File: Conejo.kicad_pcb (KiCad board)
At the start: 4 copper layers, 130.3 x 112.5 mm, 104 parts, among them J1 BATT, J2 HRO_TYPE-C-31-M-12, J3 JTAG_TC2030, J4 RGB, Q1 2N7002, Q2 2N7002, Q3 AO3407, SW1 POWER, SW10 MX Hotswap, SW11 MX Hotswap, SW12 MX Hotswap, SW13 MX Hotswap, SW14 MX Hotswap, SW15 MX Hotswap, SW16 MX Hotswap, SW17 MX Hotswap, SW18 MX Hotswap, SW19 MX Hotswap, SW2 MX Hotswap, SW20 MX Hotswap, SW21 MX Hotswap, SW22 MX Hotswap, SW23 MX Hotswap, SW24 MX Hotswap, SW25 MX Hotswap, SW26 MX Hotswap, SW27 MX Hotswap, SW28 MX Hotswap, SW29 RESET, SW3 MX Hotswap, SW4 MX Hotswap, SW5 MX Hotswap, SW6 MX Hotswap, SW7 MX Hotswap, SW8 MX Hotswap, SW9 MX Hotswap, U1 BQ24075RGT, U2 MAX17048, U3 SRV05-4, U4 MS88SF3

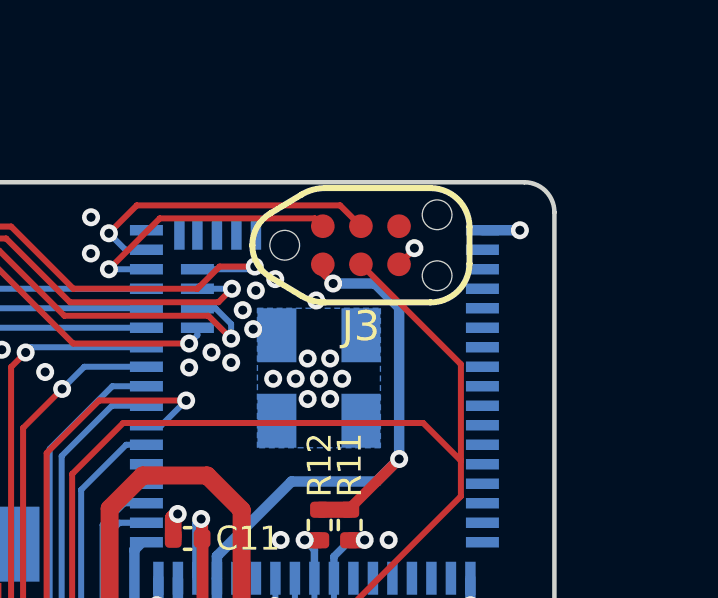
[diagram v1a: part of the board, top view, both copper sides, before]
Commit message: refactor(pcb): Update paths to 3D models, whole board .STEP
Delete EVQPU-LC-02K.STEP
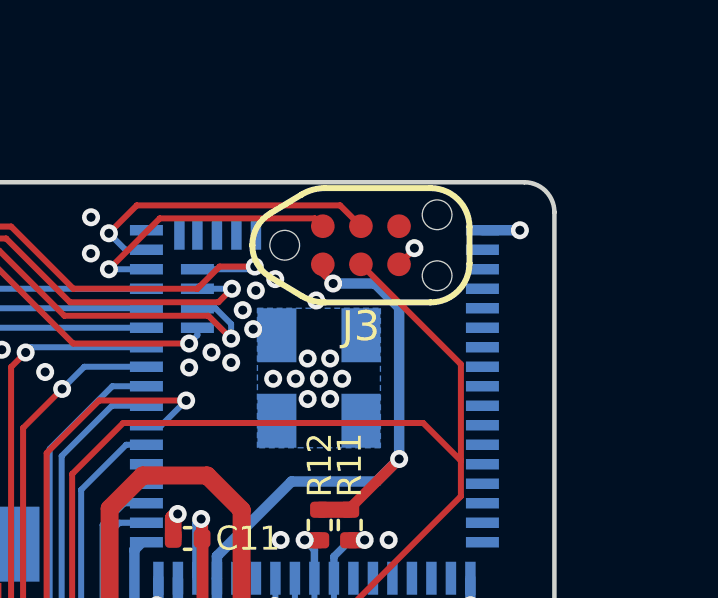
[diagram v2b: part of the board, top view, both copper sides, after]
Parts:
- U4: value MS88SF3 -> MS88SF3 nRF52840 Module
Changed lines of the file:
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@@
     (fp_arc (start 2.319501 -1.9055) (mid 3.23874 -1.524738) (end 3.6195 -0.605499) (layer "F.SilkS") (width 0.2))
     (fp_arc (start -3.6195 -0.008049) (mid -3.461104 -0.610529) (end -3.026877 -1.057203) (layer "F.SilkS") (width 0.2))
-    (fp_arc (start 3.6195 0.605498) (mid 3.23874 1.524738) (end 2.3195 1.9055) (layer "F.SilkS") (width 0.2))
+    (fp_arc (start 3.6195 0.605498) (mid 3.238739 1.524738) (end 2.3195 1.9055) (layer "F.SilkS") (width 0.2))
     (fp_arc (start -1.976732 -1.690178) (mid -1.604252 -1.850667) (end -1.202392 -1.9055) (layer "F.SilkS") (width 0.2))
     (fp_arc (start -1.202392 1.9055) (mid -1.604252 1.850667) (end -1.976732 1.690178) (layer "F.SilkS") (width 0.2))
@@
       (effects (font (size 0.4 0.4) (thickness 0.06)) (justify mirror))
     )
+    (fp_line (start -2.1 0.95) (end -2.1 1.56) (layer "B.SilkS") (width 0.12))
     (fp_line (start -2.1 1.56) (end 0.8 1.56) (layer "B.SilkS") (width 0.12))
-    (fp_line (start -2.1 0.95) (end -2.1 1.56) (layer "B.SilkS") (width 0.12))
     (fp_line (start 0 -1.56) (end -0.8 -1.56) (layer "B.SilkS") (width 0.12))
     (fp_line (start 0 -1.56) (end 0.8 -1.56) (layer "B.SilkS") (width 0.12))
+    (fp_line (start -2.05 1.7) (end -2.05 -1.7) (layer "B.CrtYd") (width 0.05))
     (fp_line (start 2.05 1.7) (end -2.05 1.7) (layer "B.CrtYd") (width 0.05))
     (fp_line (start -2.05 -1.7) (end 2.05 -1.7) (layer "B.CrtYd") (width 0.05))
     (fp_line (start 2.05 -1.7) (end 2.05 1.7) (layer "B.CrtYd") (width 0.05))
-    (fp_line (start -2.05 1.7) (end -2.05 -1.7) (layer "B.CrtYd") (width 0.05))
+    (fp_line (start -0.4 1.45) (end 0.8 1.45) (layer "B.Fab") (width 0.1))
+    (fp_line (start -0.8 -1.45) (end -0.8 1.05) (layer "B.Fab") (width 0.1))
+    (fp_line (start 0.8 -1.45) (end -0.8 -1.45) (layer "B.Fab") (width 0.1))
     (fp_line (start -0.8 1.05) (end -0.4 1.45) (layer "B.Fab") (width 0.1))
     (fp_line (start 0.8 1.45) (end 0.8 -1.45) (layer "B.Fab") (width 0.1))
-    (fp_line (start 0.8 -1.45) (end -0.8 -1.45) (layer "B.Fab") (width 0.1))
-    (fp_line (start -0.8 -1.45) (end -0.8 1.05) (layer "B.Fab") (width 0.1))
-    (fp_line (start -0.4 1.45) (end 0.8 1.45) (layer "B.Fab") (width 0.1))
     (pad "1" smd roundrect (at -1.175 0.95 270) (size 1.25 0.6) (layers "B.Cu" "B.Paste" "B.Mask") (roundrect_rratio 0.25)
       (net 103 "unconnected-(U3-Pad1)") (pinfunction "IO1") (pintype "passive"))
@@
       (effects (font (size 1 1) (thickness 0.15)) (justify mirror))
     )
-    (fp_text value "MS88SF3" (at 2.14 -12.385) (layer "B.Fab")
+    (fp_text value "MS88SF3 nRF52840 Module" (at 2.14 -12.385) (layer "B.Fab")
       (effects (font (size 1 1) (thickness 0.15)) (justify mirror))
     )
@@
     (fp_line (start 5 7) (end 7 7) (layer "Dwgs.User") (width 0.15))
     (fp_line (start 7 -7) (end 7 -5) (layer "Dwgs.User") (width 0.15))
+    (fp_line (start -5 7) (end -7 7) (layer "Dwgs.User") (width 0.15))
     (fp_line (start -7 7) (end -7 5) (layer "Dwgs.User") (width 0.15))
     (fp_line (start -5 7) (end -7 7) (layer "Dwgs.User") (width 0.15))
     (fp_line (start 5 -7) (end 7 -7) (layer "Dwgs.User") (width 0.15))
     (fp_line (start 7 5) (end 7 7) (layer "Dwgs.User") (width 0.15))
-    (fp_line (start -5 7) (end -7 7) (layer "Dwgs.User") (width 0.15))
     (fp_line (start -7 7) (end -7 5) (layer "Dwgs.User") (width 0.15))
     (fp_rect (start -14.2875 9.525) (end 14.2875 -9.525) (layer "Dwgs.User") (width 0.12) (fill none))
@@
     (fp_arc (start 6.5 4.5) (mid 5.767767 6.267767) (end 4 7) (layer "B.CrtYd") (width 0.127))
     (fp_line (start 5.3 7) (end 5.3 2.6) (layer "F.CrtYd") (width 0.127))
+    (fp_line (start -6.5 0.6) (end -2.4 0.6) (layer "F.CrtYd") (width 0.127))
     (fp_line (start -0.4 2.6) (end 5.3 2.6) (layer "F.CrtYd") (width 0.127))
-    (fp_line (start -6.5 0.6) (end -2.4 0.6) (layer "F.CrtYd") (width 0.127))
     (fp_line (start -6.5 4.5) (end -6.5 0.6) (layer "F.CrtYd") (width 0.127))
     (fp_line (start 5.3 7) (end -4 7) (layer "F.CrtYd") (width 0.127))
@@
     (pad "" smd rect (at 5.815 5.08 255) (size 2.55 2.5) (layers "F.Paste" "F.Mask"))
     (pad "" np_thru_hole circle (at 0 0 255) (size 3.9878 3.9878) (drill 3.9878) (layers *.Cu *.Mask))
-    (pad "" smd rect (at -7.085 2.54 75) (size 2.55 2.5) (layers "F.Paste" "F.Mask"))
     (pad "" smd rect (at -5.815 5.08 255) (size 2.55 2.5) (layers "B.Paste" "B.Mask"))
     (pad "" smd rect (at 7.085 2.54 255) (size 2.55 2.5) (layers "B.Paste" "B.Mask"))
     (pad "" smd rect (at 5.815 5.08 255) (size 2.55 2.5) (layers "F.Paste" "F.Mask"))
+    (pad "" smd rect (at -7.085 2.54 75) (size 2.55 2.5) (layers "F.Paste" "F.Mask"))
     (pad "1" smd rect (at -5.341 5.08 255) (size 3.498 2.5) (layers "B.Cu")
       (net 40 "COL6") (pinfunction "1") (pintype "passive"))

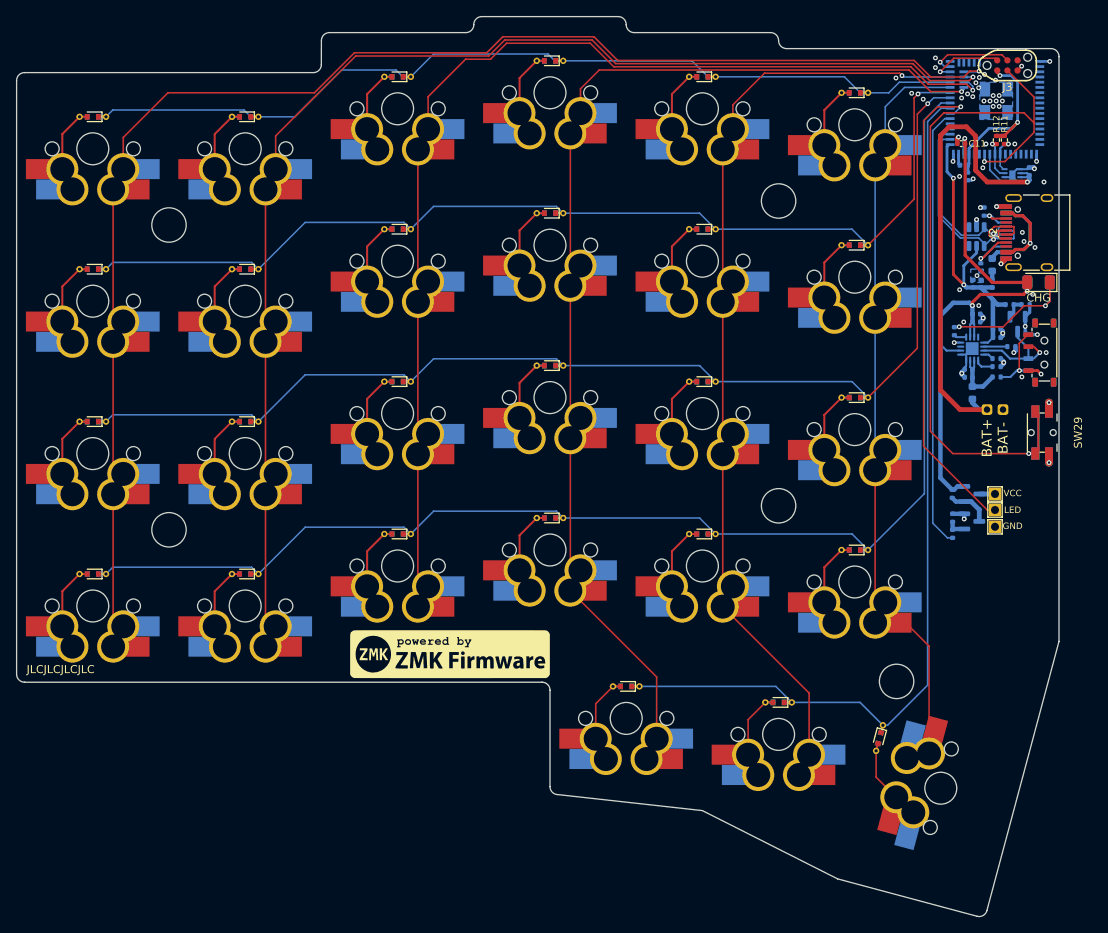
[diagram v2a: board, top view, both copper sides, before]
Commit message: feat(pcb): Version 0.2.2
- Update MS88SF3 footprint
- Create thumb cluster silksscreen
- Separate NTPH and PTH drill files
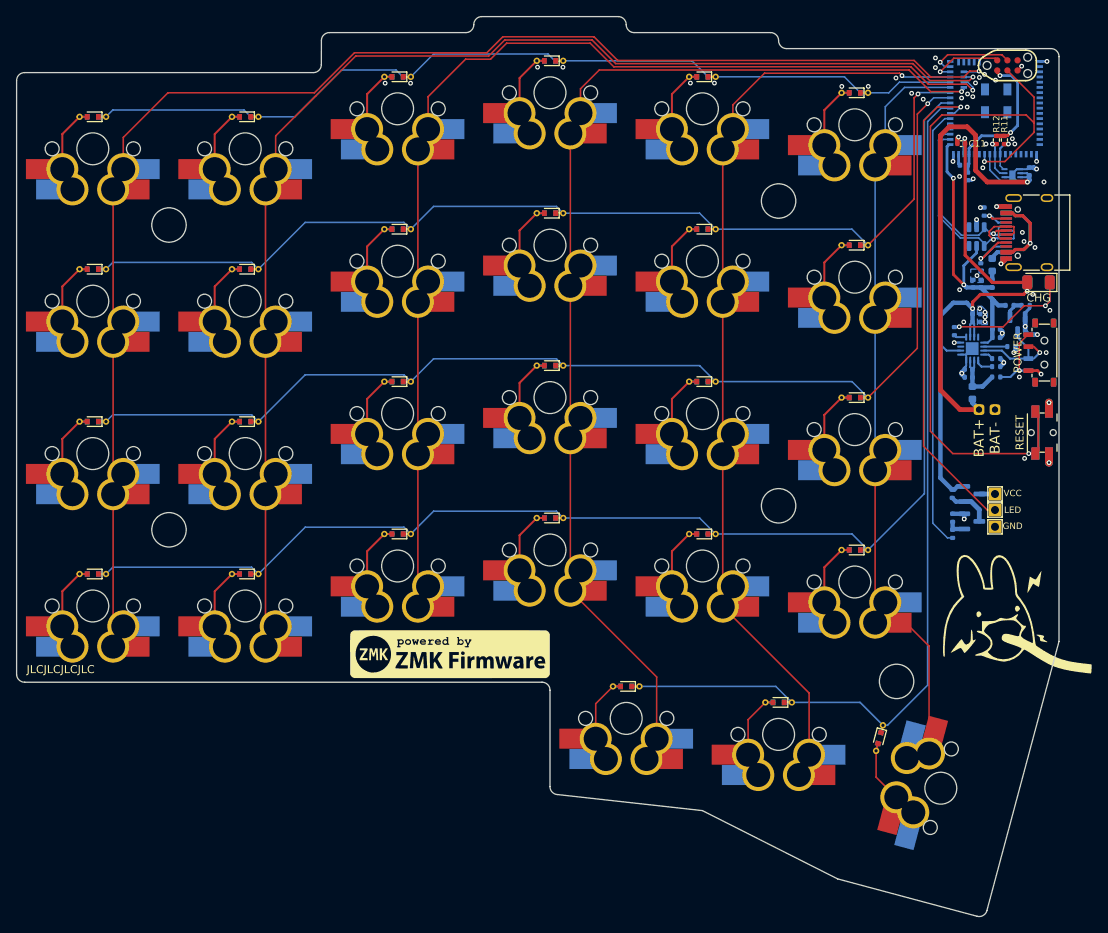
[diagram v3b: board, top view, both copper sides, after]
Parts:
- added G***: LOGO, Conejo:ConejoSilk, F.Cu at (114.8, 61.8)
- U4: value MS88SF3 nRF52840 Module -> MS88SF3; footprint Conejo:MS88SF3 -> Conejo:MS88SF3_PeteJohanson
- moved J1 1.00 mm to (111.8, 34.6)
- moved R2 0.10 mm to (116.6, 21.6)
- moved R1 0.10 mm to (114.6, 21.6)
- moved C1 0.08 mm to (112.9, 24.6)
- moved C2 0.08 mm to (112.9, 25.6)
- moved Q1 0.05 mm to (115.6, 24.0)
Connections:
- net SWDCLK renamed SWCLK
- U4 pad 61: GND -> (no net)
- U4 pad 62: GND -> (no net)
- U4 pad 63: GND -> (no net)
- U4 pad 64: GND -> (no net)
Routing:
- net +BATT: track 61.4 -> 59.4 mm
- net VDD: track 22.3 -> 21.2 mm
- net GND: track 39.8 -> 38.7 mm, vias 59 -> 64
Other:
- rule pad_to_mask_clearance: 0.05 -> 0
- board text added: "RESET"

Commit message: fix(pcb): Finalize part selection
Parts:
- L1: footprint Inductor_SMD:L_0402_1005Metric -> Inductor_SMD:L_0603_1608Metric
- moved C11 1.17 mm to (108.5, 2.52)
- moved C10 0.60 mm to (109.7, 5.97)
- moved L1 0.28 mm to (108.9, 4.33)
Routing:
- net VDDH: track 73.8 -> 72.1 mm
- net +BATT: track 59.4 -> 57.8 mm

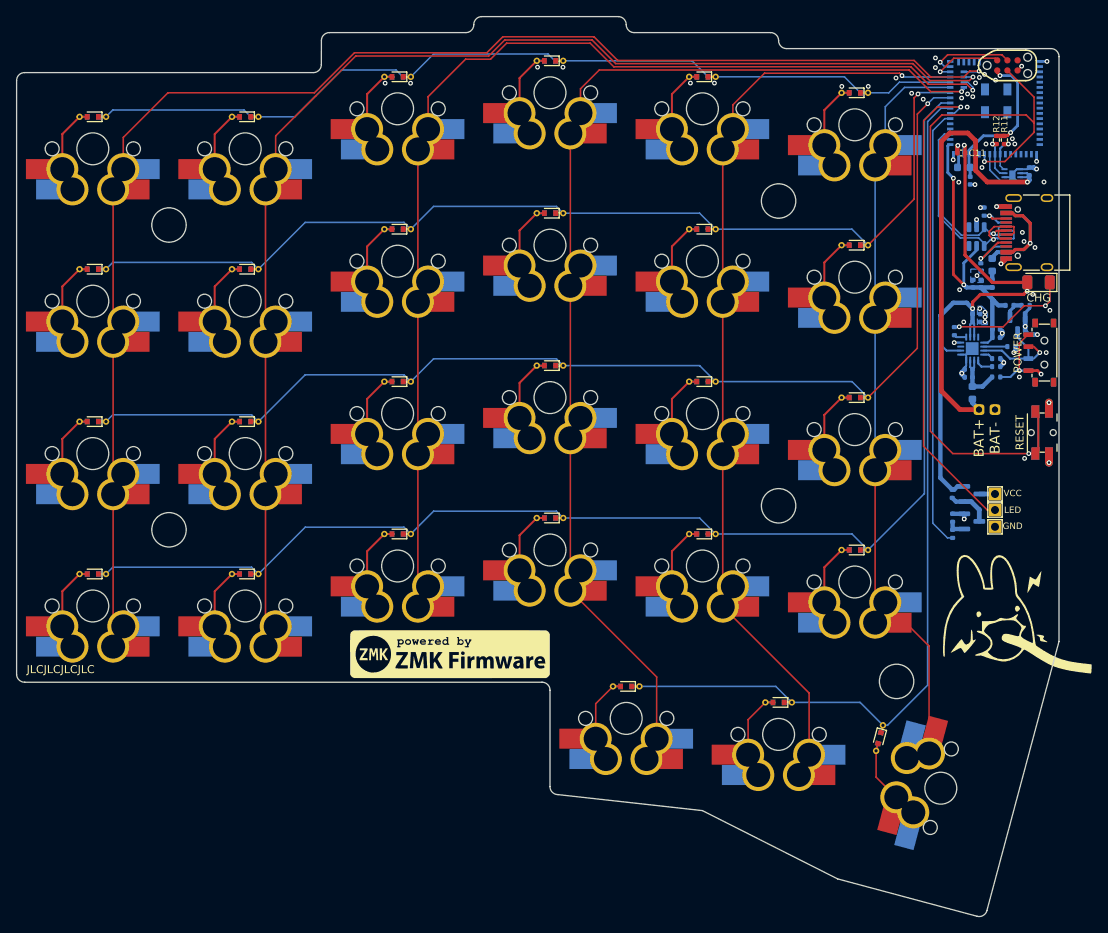
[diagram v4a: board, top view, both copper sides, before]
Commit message: feat(pcb): Version 0.2.3
- Switched vertical traces on matrix to back copper
- Added GND vias for all diodes
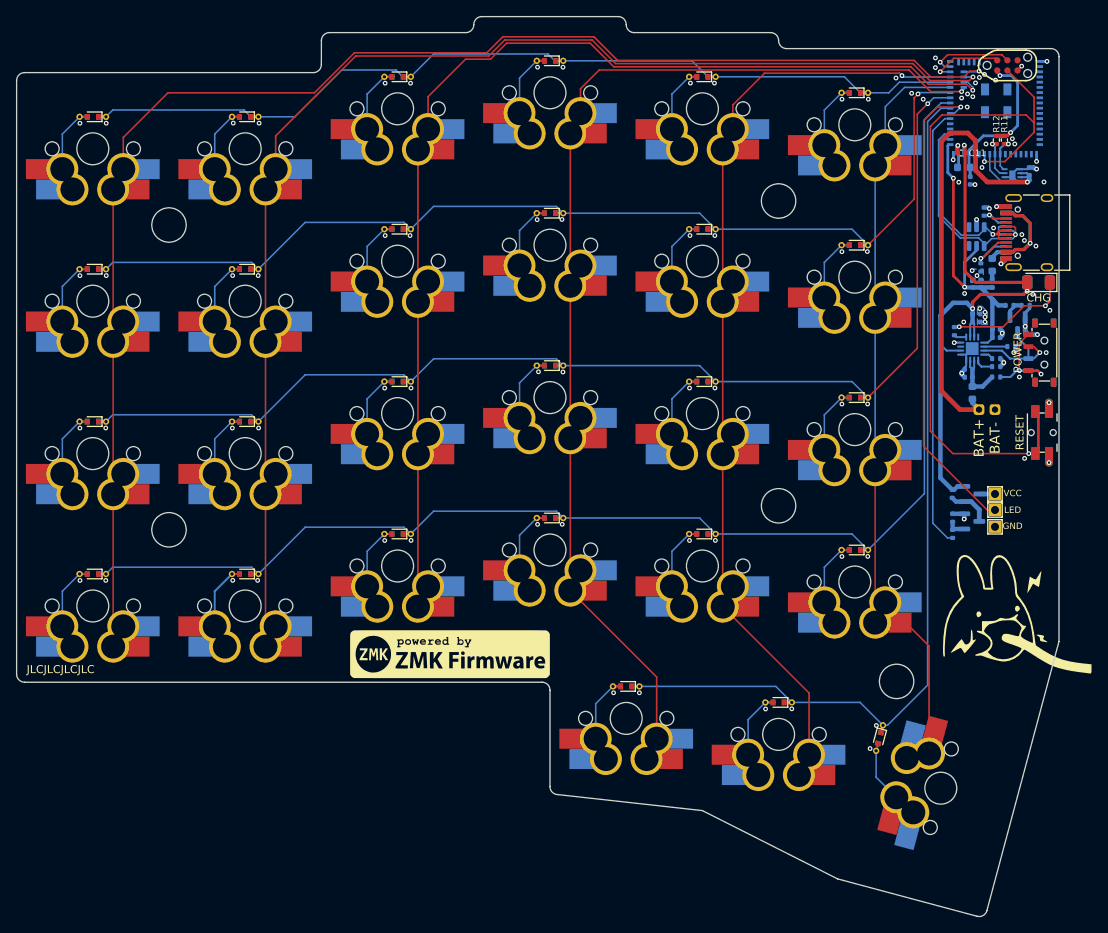
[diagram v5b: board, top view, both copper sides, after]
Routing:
- net D+: track 30.8 -> 27.7 mm
- net D-: track 27.3 -> 25.5 mm
- net VDDH: track 72.1 -> 73.3 mm
- net GND: track 38.5 -> 38.7 mm, vias 64 -> 113
